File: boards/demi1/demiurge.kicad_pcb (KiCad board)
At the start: 2 copper layers, 40.1 x 109.9 mm, 140 parts, among them J12 Micro_SD_Card_Det_Hirose_DM3AT, J2 Conn_01x06, U1 MCP6002, U10 TL072, U11 TL072, U13 CH32V307RCT6, U2 AMS1117-3.3, U3 MCP6002, U4 AW20036, U5 W25Q128JVS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

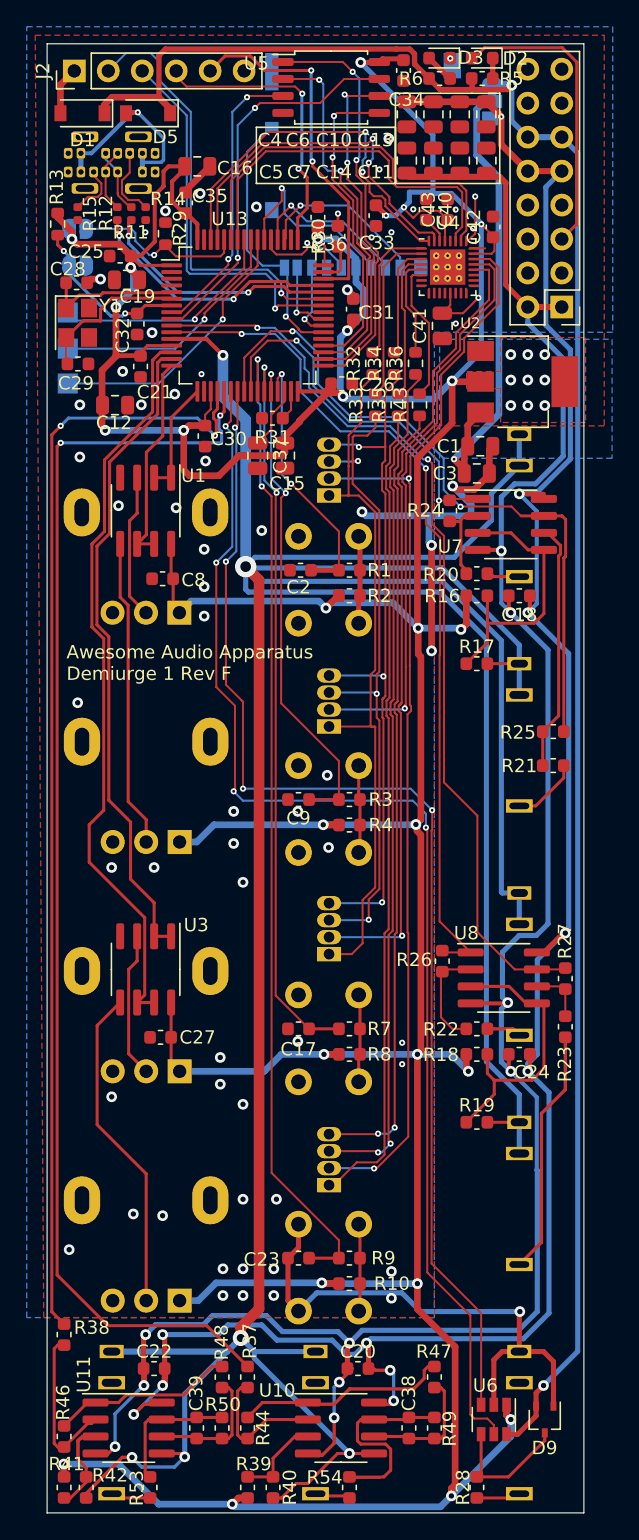
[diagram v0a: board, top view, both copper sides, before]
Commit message: Adding testpad for MCO pin, for instance to check clock speeds.
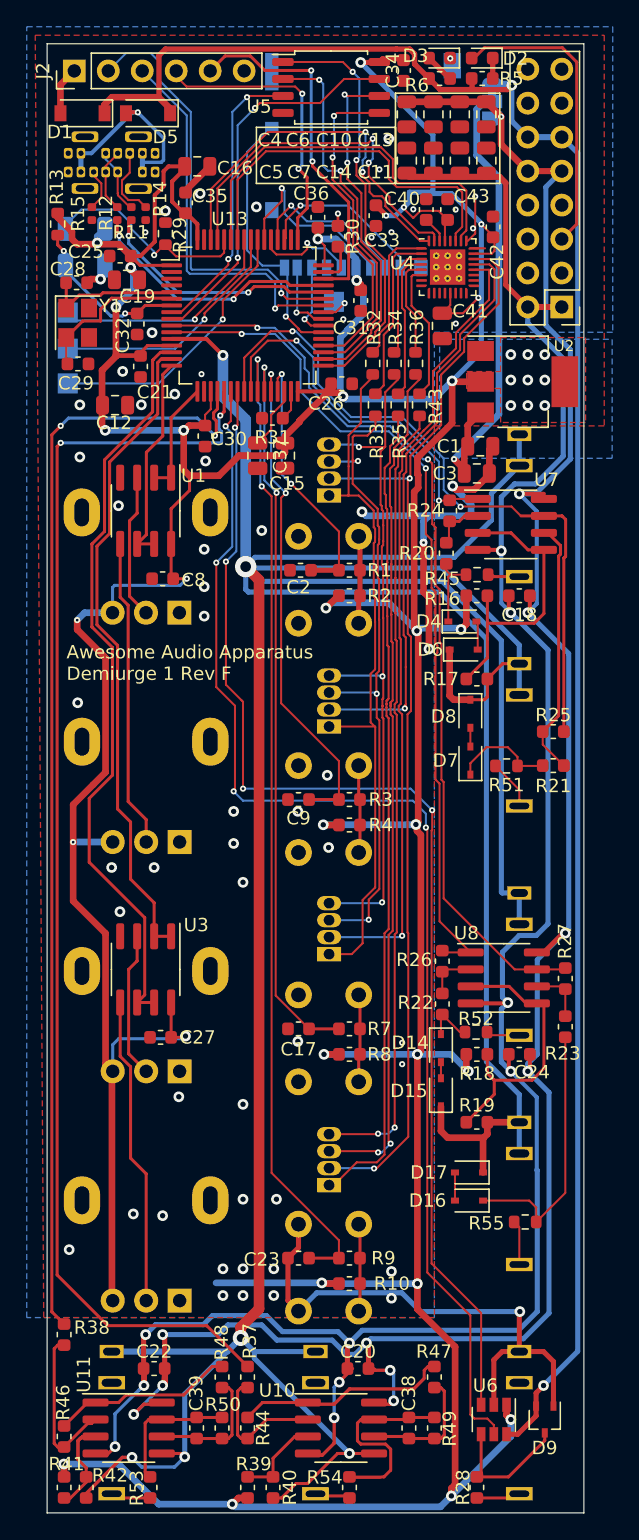
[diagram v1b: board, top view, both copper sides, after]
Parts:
- added D14: 10V, Diode_SMD:D_SOD-323, F.Cu at (105.9, 125.9)
- added D15: 10V, Diode_SMD:D_SOD-323, F.Cu at (105.9, 129.2)
- added D16: 10V, Diode_SMD:D_SOD-323, F.Cu at (108.0, 137.3)
- added D17: 10V, Diode_SMD:D_SOD-323, F.Cu at (108.0, 135.2)
- added D4: 10V, Diode_SMD:D_SOD-323, F.Cu at (107.5, 94.0)
- added D6: 10V, Diode_SMD:D_SOD-323, F.Cu at (107.6, 96.1)
- added D7: 10V, Diode_SMD:D_SOD-323, F.Cu at (108.1, 104.4)
- added D8: 10V, Diode_SMD:D_SOD-323, F.Cu at (108.1, 100.9)
- added R45: 100, Resistor_SMD:R_0603_1608Metric, F.Cu at (108.6, 90.5)
- added R51: 100, Resistor_SMD:R_0603_1608Metric, F.Cu at (110.8, 104.8)
- added R52: 100, Resistor_SMD:R_0603_1608Metric, F.Cu at (108.5, 124.7)
- added R55: 100, Resistor_SMD:R_0603_1608Metric, F.Cu at (112.2, 138.9)
- added TP4: SWO, TestPoint:TestPoint_Pad_1.5x1.5mm, B.Cu at (97.9, 70.1)
- JP2, JP3: footprint Jumper:SolderJumper-2_P1.3mm_Open_RoundedPad1.0x1.5mm -> Capacitor_SMD:C_1206_3216Metric
- moved R22 3.18 mm to (106.0, 122.6), turned to -90 degrees
- moved R20 2.75 mm to (106.3, 88.9), turned to -90 degrees
- moved R17 1.14 mm to (108.6, 98.3)
- moved R15 1.06 mm to (79.8, 63.5)
- moved C31 0.85 mm to (99.9, 70.0), turned to -90 degrees
- moved JP2 0.56 mm to (79.3, 64.6), turned to 0 degrees
- moved JP3 0.56 mm to (79.3, 67.4)
- turned R21 to 180 degrees
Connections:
- R20 pad 2: Net-(J3-PadT) -> Net-(R20-Pad2)
- R21 pad 2: Net-(J4-PadT) -> Net-(R21-Pad2)
- R22 pad 2: Net-(J5-PadT) -> Net-(R22-Pad2)
- R23 pad 2: Net-(J6-PadT) -> Net-(R23-Pad2)
- RV1 pad 1: +3V3 -> GND
- RV1 pad 3: GND -> +3V3
- RV2 pad 1: +3V3 -> GND
- RV2 pad 3: GND -> +3V3
- RV3 pad 1: +3V3 -> GND
- RV3 pad 3: GND -> +3V3
- RV4 pad 1: +3V3 -> GND
- RV4 pad 3: GND -> +3V3
- U13 pad 41: unconnected-(U13-Pad41) -> /MCO
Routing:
- net +3V3: track 392.1 -> 433.6 mm, vias 37 -> 41
- net Net-(R23-Pad2): track 0.00 -> 20.0 mm
- net GNDA: track 300.2 -> 317.7 mm
- net Net-(J6-PadT): track 18.4 -> 3.34 mm
- net Net-(R21-Pad2): track 0.00 -> 7.75 mm
- net Net-(R20-Pad2): track 0.00 -> 5.67 mm
- net Net-(R22-Pad1): track 7.90 -> 3.96 mm
- net Net-(R22-Pad2): track 0.00 -> 3.75 mm
- net BOOT0: track 13.2 -> 16.2 mm
- net /MCO: track 0.00 -> 2.70 mm, vias 0 -> 1
- net Net-(R20-Pad1): track 6.19 -> 3.89 mm
- net Net-(D4-Pad2): track 0.00 -> 2.14 mm
- net Net-(D16-Pad2): track 0.00 -> 2.10 mm
- net Net-(RV4-Pad2): track 24.5 -> 23.1 mm
- net Net-(D7-Pad2): track 0.00 -> 1.40 mm
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
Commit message: RevF order made at jlcpcb.
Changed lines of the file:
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@@
   (paper "A4")
   (title_block
-    (title "AAA Demiurge")
+    (title "AAA Demiurge 1")
+    (date "2022-08-11")
     (rev "F")
     (company "Awesome Audio Apparatus")
@@
       (drillshape 0)
       (scaleselection 1)
-      (outputdirectory "RevE/")
+      (outputdirectory "RevF/")
     )
   )
@@
     (property "Sheetname" "")
     (attr smd)
-    (fp_text reference "D2" (at -2.485 -0.03 180) (layer "F.SilkS")
+    (fp_text reference "D2" (at -2.115 -0.024 180) (layer "F.SilkS")
       (effects (font (size 1 1) (thickness 0.1524)))
     )
@@
     (property "Sheetname" "")
     (attr smd)
-    (fp_text reference "R31" (at 0 -1.43) (layer "F.SilkS")
+    (fp_text reference "R31" (at -2.6 -0.2) (layer "F.SilkS")
       (effects (font (size 1 1) (thickness 0.15)))
     )
@@
     (fp_line (start 1.6 -0.8) (end -1.6 -0.8) (layer "B.Fab") (width 0.1))
     (fp_line (start -1.6 -0.8) (end -1.6 0.8) (layer "B.Fab") (width 0.1))
-    (pad "1" smd roundrect (at -1.475 0) (size 1.15 1.8) (layers "B.Cu" "B.Paste" "B.Mask") (roundrect_rratio 0.217391)
+    (pad "1" smd roundrect (at -1.475 0) (size 1.15 1.8) (layers "B.Cu" "B.Paste" "B.Mask") (roundrect_rratio 0.2173913043)
       (net 97 "BOOT0") (pinfunction "A") (pintype "passive"))
-    (pad "2" smd roundrect (at 1.475 0) (size 1.15 1.8) (layers "B.Cu" "B.Paste" "B.Mask") (roundrect_rratio 0.217391)
+    (pad "2" smd roundrect (at 1.475 0) (size 1.15 1.8) (layers "B.Cu" "B.Paste" "B.Mask") (roundrect_rratio 0.2173913043)
       (net 1 "+3V3") (pinfunction "B") (pintype "passive"))
   )
@@
     (property "Sheetname" "")
     (attr smd)
-    (fp_text reference "J12" (at -0.075 9.525) (layer "B.SilkS")
+    (fp_text reference "J12" (at -0.075 9.525) (layer "B.SilkS") hide
       (effects (font (size 1 1) (thickness 0.15)) (justify mirror))
     )
@@
     (property "Sheetname" "")
     (attr exclude_from_pos_files)
-    (fp_text reference "TP4" (at 0 1.648) (layer "B.SilkS")
+    (fp_text reference "TP4" (at 2.3 0.3) (layer "B.SilkS")
       (effects (font (size 1 1) (thickness 0.15)) (justify mirror))
     )
@@
     (fp_line (start -1.6 -0.8) (end -1.6 0.8) (layer "B.Fab") (width 0.1))
     (fp_line (start -1.6 0.8) (end 1.6 0.8) (layer "B.Fab") (width 0.1))
-    (pad "1" smd roundrect (at -1.475 0 180) (size 1.15 1.8) (layers "B.Cu" "B.Paste" "B.Mask") (roundrect_rratio 0.217391)
+    (pad "1" smd roundrect (at -1.475 0 180) (size 1.15 1.8) (layers "B.Cu" "B.Paste" "B.Mask") (roundrect_rratio 0.2173913043)
       (net 18 "GND") (pinfunction "A") (pintype "passive"))
-    (pad "2" smd roundrect (at 1.475 0 180) (size 1.15 1.8) (layers "B.Cu" "B.Paste" "B.Mask") (roundrect_rratio 0.217391)
+    (pad "2" smd roundrect (at 1.475 0 180) (size 1.15 1.8) (layers "B.Cu" "B.Paste" "B.Mask") (roundrect_rratio 0.2173913043)
       (net 87 "NRST") (pinfunction "B") (pintype "passive"))
   )
@@
   (gr_line (start 116.586 50.8) (end 116.586 160.655) (layer "Edge.Cuts") (width 0.05))
   (gr_line (start 76.454 50.8) (end 116.586 50.8) (layer "Edge.Cuts") (width 0.05))
-  (gr_text "Awesome Audio Apparatus\nDemiurge 1 Rev F" (at 102.9 72.1) (layer "B.SilkS")
+  (gr_text "Awesome Audio Apparatus\nDemiurge 1 Rev F" (at 102.9 72.9) (layer "B.SilkS")
     (effects (font (size 1 1) (thickness 0.15)) (justify left mirror))
   )

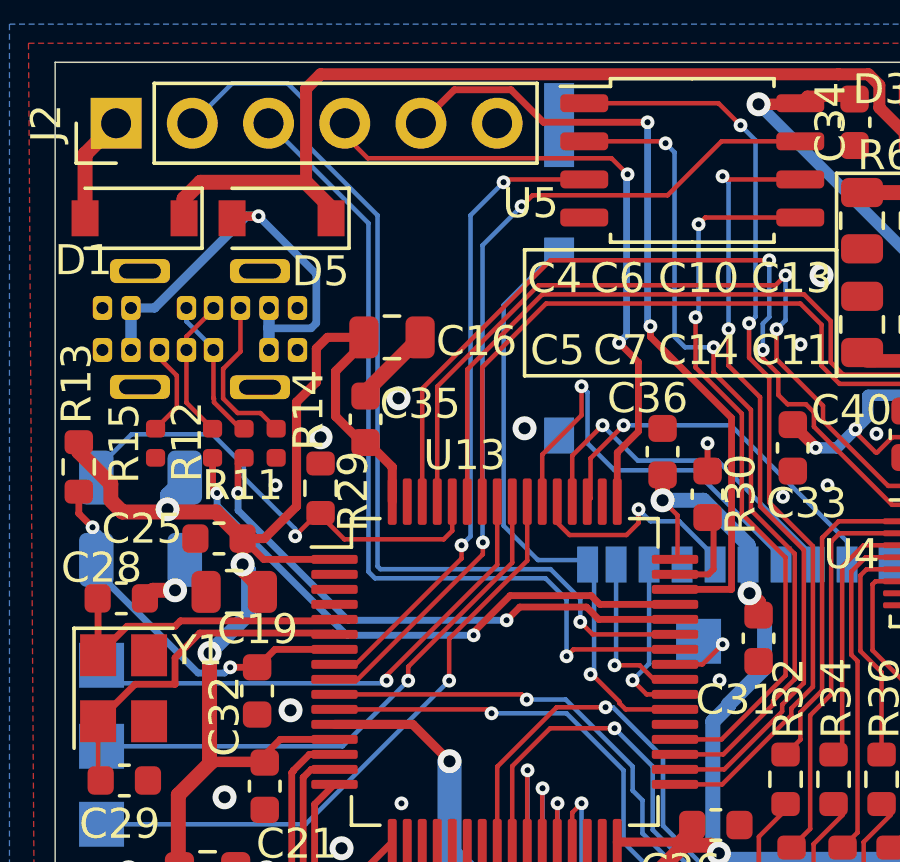
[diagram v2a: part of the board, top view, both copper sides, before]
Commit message: Forgot I2C resistors. Grrr...
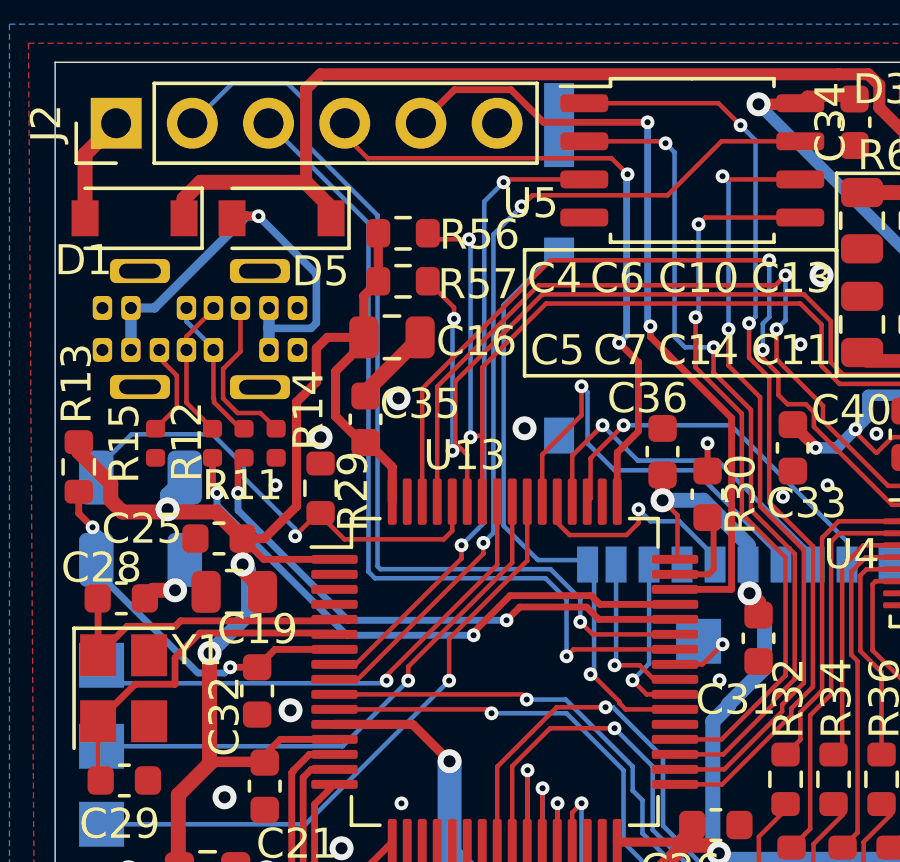
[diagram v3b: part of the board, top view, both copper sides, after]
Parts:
- added R56: 3k3, Resistor_SMD:R_0603_1608Metric, F.Cu at (88.0, 56.5)
- added R57: 3k3, Resistor_SMD:R_0603_1608Metric, F.Cu at (88.0, 58.1)
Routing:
- net SCL: track 28.1 -> 37.0 mm, vias 0 -> 2
- net SDA: track 29.1 -> 35.8 mm, vias 0 -> 2
- net +3V3: track 433.6 -> 437.3 mm

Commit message: RevG using STM32F446.
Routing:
- net +3V3: track 437.3 -> 429.4 mm
- net AD4: track 56.2 -> 56.7 mm
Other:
- board text added: "Awesome Audio Apparatus Demiurge 1 Rev G"
- board text removed: "Awesome Audio Apparatus Demiurge 1 Rev F"
